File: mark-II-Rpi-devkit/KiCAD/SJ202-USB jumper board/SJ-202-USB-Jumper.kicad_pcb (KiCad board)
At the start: 2 copper layers, 40 x 21.5 mm, 3 parts, among them J1 USB_A, J2 USB3150-30-130-A, J3 Conn_01x05

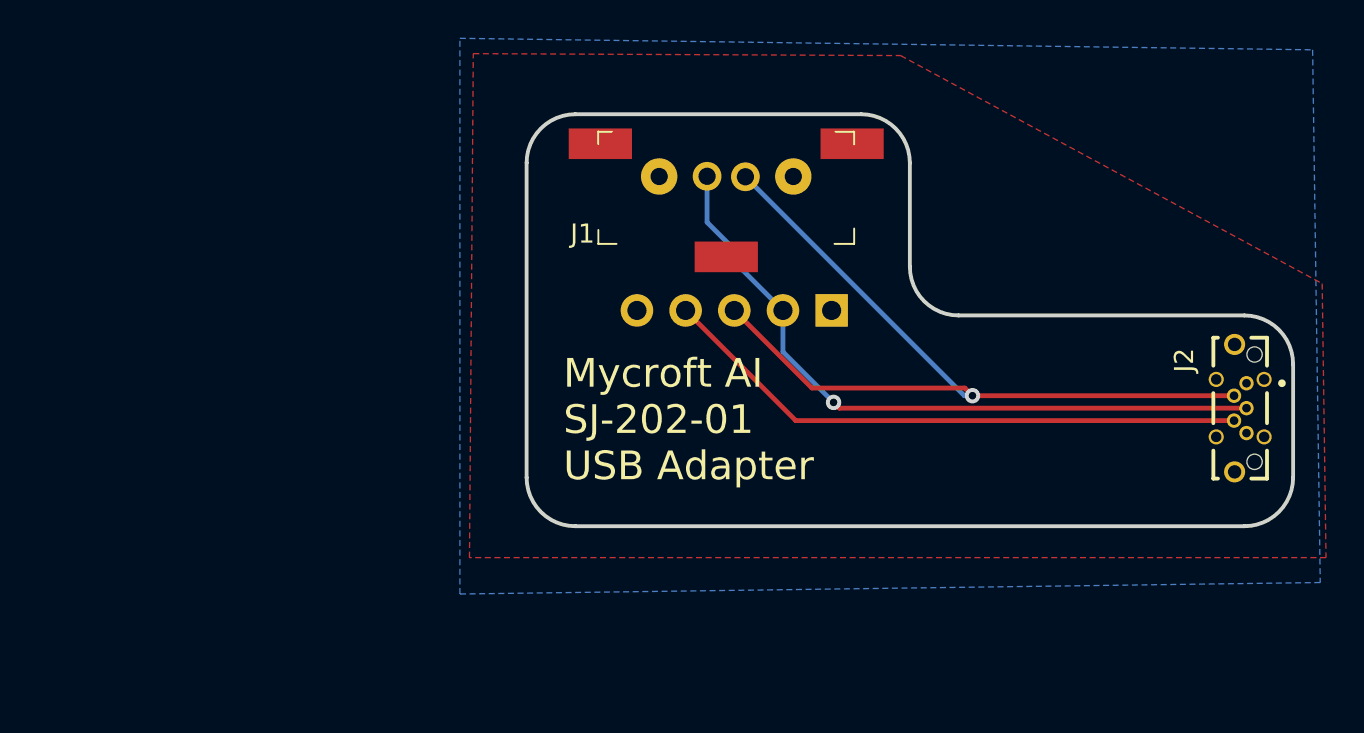
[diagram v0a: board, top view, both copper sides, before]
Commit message: SJ201 - Removed CM108b soundcard, added in I2S to Line out, ATTin402. Moved holes in layout. SJ202 - extened length to plug into USB2.0 port
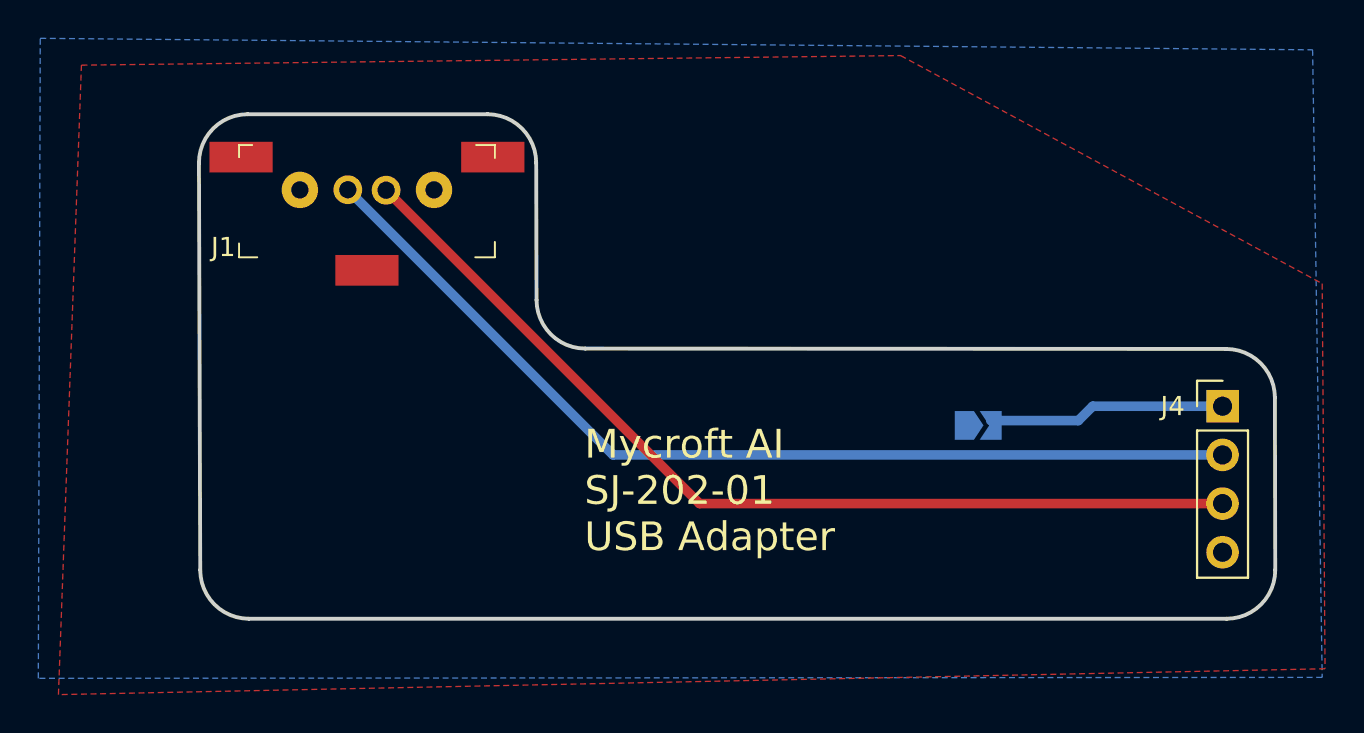
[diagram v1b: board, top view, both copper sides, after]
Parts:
- removed J3: Conn_01x05, Connector_PinHeader_2.54mm:PinHeader_1x05_P2.54mm_Vertical
- added J4: Conn_01x04, Connector_PinHeader_2.54mm:PinHeader_1x04_P2.54mm_Vertical, F.Cu at (74.3, 67.3)
- J2: value USB3150-30-130-A -> 5vJumper; footprint libraries:GCT_USB3150-30-130-A -> Jumper:SolderJumper-2_P1.3mm_Open_TrianglePad1.0x1.5mm; moved to B.Cu
- moved J1 18.8 mm to (29.6, 53.3)
- moved J2 13.4 mm to (61.5, 68.3), turned to 0 degrees
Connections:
- J2 pad 2: /D- -> /5vJump
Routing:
- net /ID: track 31.1 -> 0.00 mm, vias 1 -> 0
- net /D+: track 36.2 -> 51.6 mm, vias 1 -> 0
- net /5vJump: track 0.00 -> 12.6 mm
- net /D-: track 44.5 -> 50.6 mm, vias 1 -> 0
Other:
- board size 40 x 21.5 mm -> 56.2 x 26.3 mm
- net class Default: clearance 0.1 -> 0.2; trace_width 0.25 -> 0.5
- net class Signal Wire: clearance 0.1 -> 0.2; trace_width 0.25 -> 0.5
- rule trace_clearance: 0.1 -> 0.2
- board text added: "5V D+ D- GND"
- board text removed: "GND ID D- D+ 5V"
